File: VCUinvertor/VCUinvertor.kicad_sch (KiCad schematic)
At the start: 127 parts, among them J7 PowerSupply, J8 CAN_NXP, J9 BACKLIGHT, Q11 MMBT3904, Q12 IRLML6402, Q13 MMBT3904, Q14 IRLML6402, Q17 MMBT3904, Q18 MMBT3904, Q19 MMBT3904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

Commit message: FirstLayout_Completed
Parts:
- removed NXP11: NXP11, Connector_PinHeader_2.54mm:PinHeader_2x08_P2.54mm_Vertical, symbol Connector_Generic:Conn_02x10_Odd_Even
- removed NXP13: NXP13, Connector_PinHeader_2.54mm:PinHeader_2x10_P2.54mm_Vertical, symbol Connector_Generic:Conn_02x10_Odd_Even
- removed NXP14: NXP14, Connector_PinHeader_2.54mm:PinHeader_2x10_P2.54mm_Vertical, symbol Connector_Generic:Conn_02x10_Odd_Even
- removed Q11, Q13, Q17, Q18, Q19, Q23, Q25, Q27, Q29, Q41: MMBT3904, Package_TO_SOT_SMD:SOT-23, symbol Transistor_BJT:MMBT3904
- removed Q12, Q14, Q20, Q21, Q22, Q24, Q26, Q28, Q30, Q42: IRLML6402, Package_TO_SOT_SMD:SOT-23, symbol Transistor_FET:IRLML6402
- removed R29, R32, R33, R36, R41, R43, R45, R50, R51, R52, R53, R56, R57, R60, R61, R65, R68, R89, R92: 10k, Resistor_SMD:R_0805_2012Metric, symbol Device:R_Small
- removed R30, R34, R42, R44, R46, R54, R58, R62, R66, R90: 100k, Resistor_SMD:R_0805_2012Metric, symbol Device:R_Small
- removed R31, R35, R47, R48, R49, R55, R59, R67, R91: 100, Resistor_SMD:R_0805_2012Metric, symbol Device:R_Small
- added NXP11: NXP11, Connector_PinHeader_2.54mm:PinHeader_2x08_P2.54mm_Vertical, symbol Connector_Generic:Conn_02x08_Odd_Even
- added NXP13: NXP13, Connector_PinHeader_2.54mm:PinHeader_2x08_P2.54mm_Vertical, symbol Connector_Generic:Conn_02x08_Odd_Even
- added NXP14: NXP14, Connector_PinHeader_2.54mm:PinHeader_2x08_P2.54mm_Vertical, symbol Connector_Generic:Conn_02x08_Odd_Even
- added Q1, Q10, Q2, Q3, Q4, Q5, Q6, Q7, Q8, Q9: 2N7002, Package_TO_SOT_SMD:SOT-23, symbol Transistor_FET:2N7002
- added R10, R11, R12, R13, R14, R15, R16, R17, R18, R19, R20, R21, R22, R5, R6, R7, R8, R9: 10k, Resistor_SMD:R_0805_2012Metric, symbol Device:R_Small
- NXP10, NXP12: footprint Connector_PinHeader_2.54mm:PinHeader_2x08_P2.54mm_Vertical -> Connector_PinHeader_2.54mm:PinHeader_2x10_P2.54mm_Vertical
- R63: value 100 -> 10k
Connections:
- net V-1 is gone; now on net GND: JU1.4 (Pin_4)
- net V-2 is gone; now on net GND: JU2.4 (Pin_4)
- net +12V: now also NXP13.1 (Pin_1), R10.1, R12.1, R14.1, R16.1, R18.1, R20.1, R22.1, R6.1, R8.1
- net ACC1: now also Q2.3 (D), R6.2
- net ACC2: now also R64.2, Q1.3 (D)
- net BREAKLIGHT: now also NXP13.2 (Pin_2)
- net ECO1: now also Q3.3 (D), R8.2
- net ECO2: now also Q7.3 (D), R16.2
- net FWD1: now also Q5.3 (D), R12.2
- net FWD2: now also Q9.3 (D), R20.2
- net GND: now also U1.15 (GND), NXP13.13 (Pin_13), Q1.2 (S), Q10.2 (S), Q2.2 (S), Q3.2 (S), Q4.2 (S), Q5.2 (S), Q6.2 (S), Q7.2 (S), Q8.2 (S), Q9.2 (S)
- net H_Brk1: now also Q4.3 (D), R10.2
- net H_Brk2: now also Q8.3 (D), R18.2
- net NXP_ACC01: now also NXP12.20 (Pin_20), R5.1
- net NXP_ACC02: now also NXP10.14 (Pin_14), R63.1
- net NXP_BRK01: now also NXP12.5 (Pin_5), R9.1
- net NXP_BRK02: now also NXP10.10 (Pin_10), R17.1
- net NXP_ECO01: now also NXP12.18 (Pin_18), R7.1
- net NXP_ECO02: now also NXP10.12 (Pin_12), R15.1
- net NXP_FWD01: now also NXP12.4 (Pin_4), R11.1
- net NXP_FWD02: now also NXP10.8 (Pin_8), R19.1
- net NXP_REV01: now also NXP12.2 (Pin_2), R13.1
- net NXP_REV02: now also NXP10.6 (Pin_6), R21.1
- net NXP_TPSOUT01: now also NXP14.1 (Pin_1)
- net NXP_TPSOUT02: now also NXP14.3 (Pin_3)
- net REV1: now also Q6.3 (D), R14.2
- net REV2: now also Q10.3 (D), R22.2
- net Rx_UART01: now also NXP12.8 (Pin_8); no longer NXP12.2 (Pin_2)
- net Rx_UART02: now also NXP11.2 (Pin_2)
- net Tx_UART01: now also NXP12.6 (Pin_6); no longer NXP12.3 (Pin_3)
- net Tx_UART02: now also NXP11.3 (Pin_3)
- net at R63.2: now also Q1.1 (G)
- net V+1: no longer names the net of JU1.1 (Pin_1)
- net V+2: no longer names the net of JU2.1 (Pin_1)
- new net: Q7.1 (G), R15.2
- new net: Q6.1 (G), R13.2
- new net: Q9.1 (G), R19.2
- new net: Q4.1 (G), R9.2
- new net: Q5.1 (G), R11.2
- new net: Q2.1 (G), R5.2
- new net: Q3.1 (G), R7.2
- new net: Q10.1 (G), R21.2
- new net: Q8.1 (G), R17.2
- no-connect marks 85 -> 95
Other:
- moved on the sheet: CA1, J8, NXP10, NXP12, NXP15, R63, R64

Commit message: Pyy & Pzz pin assignment
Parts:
- renumbered J8 to J21
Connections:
- net Pyy: now also NXP11.16 (Pin_16)
- net Pzz: now also NXP11.4 (Pin_4)
- no-connect marks 95 -> 93
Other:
- note added: "J13 - pin: 1 & 15 (12V) J13 - pin: 13 (GND)"
- note removed: "J13 - 1 & 15 (12V) J13 - 13 (GND)"
- moved on the sheet: C1, C10, C11, C12, C2, C5, C6, C7, C8, C9, DAC1, JU1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

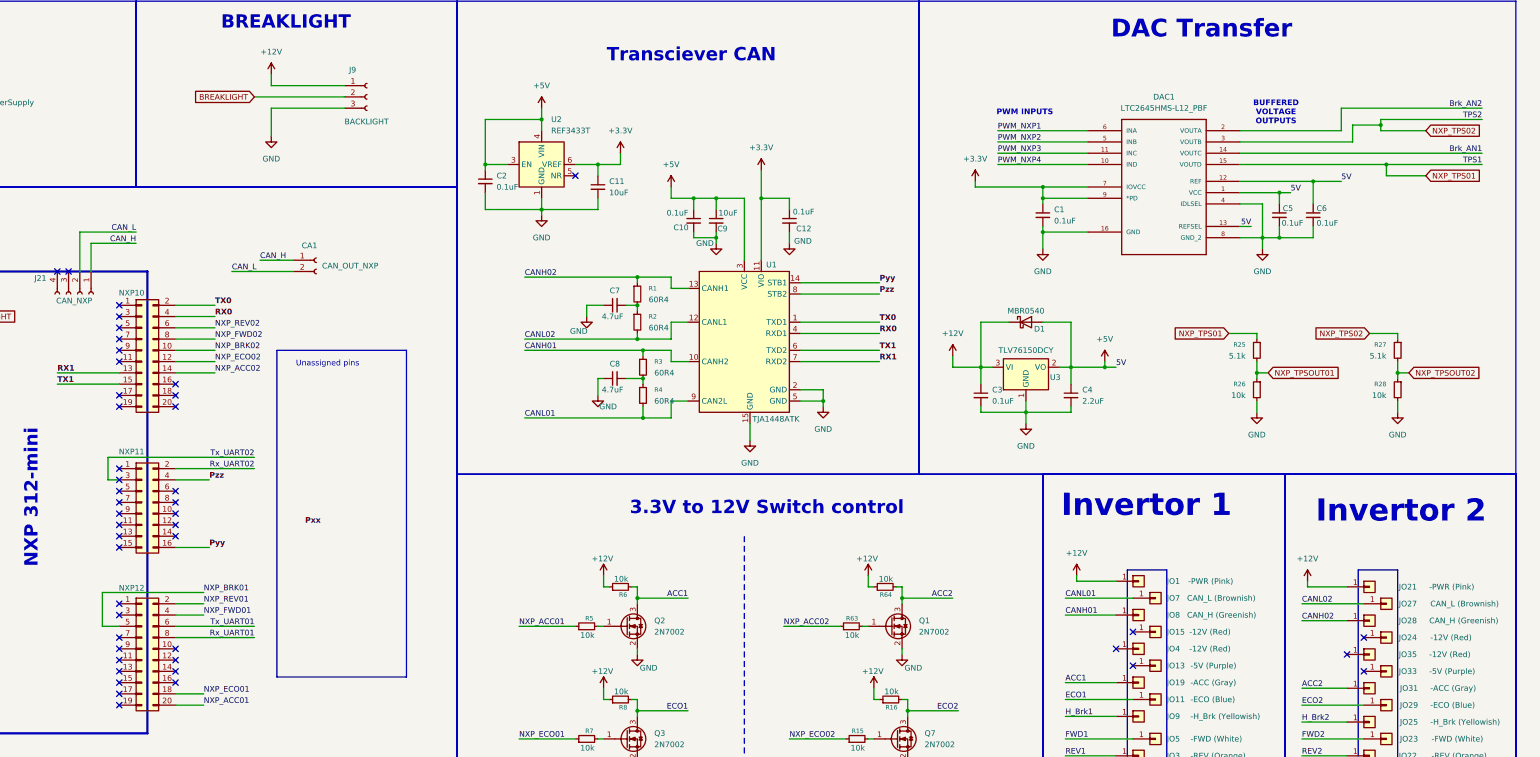
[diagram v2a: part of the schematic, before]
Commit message: Added datasheets for MOS
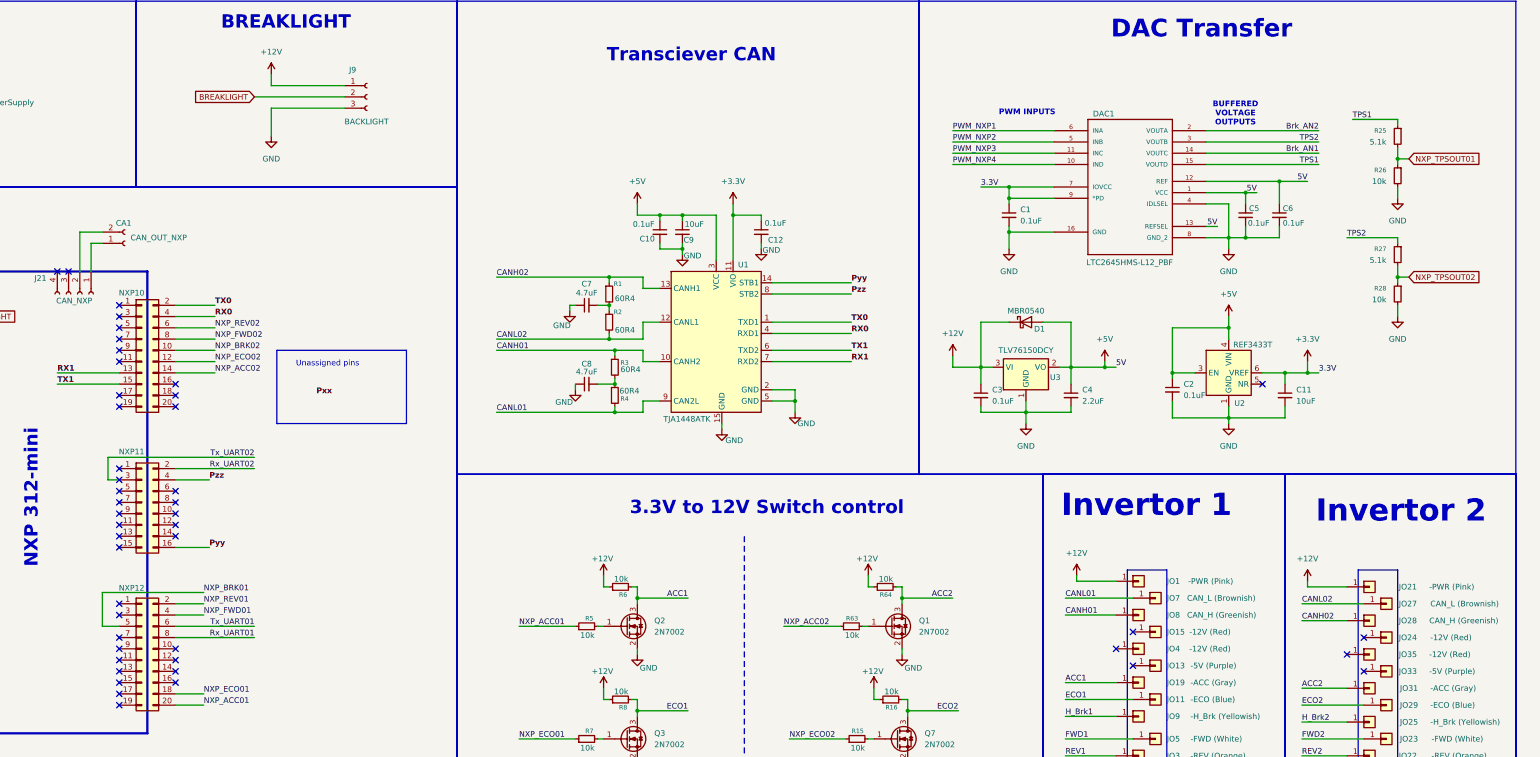
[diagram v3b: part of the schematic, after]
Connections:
- net CAN_H: no longer names the net of CA1.1 (Pin_1), J21.1 (Pin_1)
- net CAN_L: no longer names the net of CA1.2 (Pin_2), J21.2 (Pin_2)
- net NXP_TPS01 renamed TPS1
- net NXP_TPS02 renamed TPS2
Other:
- moved on the sheet: C1, C10, C11, C12, C2, C5, C6, C7, C8, C9, CA1, DAC1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

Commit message: LastCorrection_ToBeChecked
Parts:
- J7: footprint Connector_Phoenix_MSTB:PhoenixContact_MSTBVA_2,5_2-G-5,08_1x02_P5.08mm_Vertical -> Connector_JST:JST_PH_B2B-PH-K_1x02_P2.00mm_Vertical
- JO1, JO21: value -PWR (Pink) -> PWR (Pink)
- JO11, JO29: value -ECO (Blue) -> ECO (Blue)
- JO12, JO32: value -TPS (Green) -> TPS (Green)
- JO13, JO33: value -5V (Purple) -> 5V (Purple)
- JO14, JO26, JO34, JO6: value -GND (Black) -> GND (Black)
- JO15, JO24, JO35, JO4: value -12V (Red) -> 12V (Red)
- JO19, JO31: value -ACC (Gray) -> ACC (Gray)
- JO22, JO3: value -REV (Orange) -> REV (Orange)
- JO23, JO5: value -FWD (White) -> FWD (White)
- JO25, JO9: value -H_Brk (Yellowish) -> H_Brk (Yellowish)
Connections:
- net PWM_NXP1: now also NXP15.11 (Pin_11); no longer NXP15.9 (Pin_9)
- net PWM_NXP2: now also NXP15.9 (Pin_9); no longer NXP15.11 (Pin_11)
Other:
- moved on the sheet: C10, C12, C7, C8, C9, R1, R2, R3, R4, U1

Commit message: Block diagram cleanup
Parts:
- J9: value BACKLIGHT -> BREAKLIGHT
- renumbered J21 to CA0
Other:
- note added: "1. PWR(7): Controller power supply (input). ※Pink 2. REV_SW(14): Reverse switch input. ※Orange 3. GND(6): Signal return or power supply return. ※Black 4. FWD(12): Forward switch or can be enabled as High speed switch function. ※White 5. Throttle(3): Throttle analog input, 0-5V. ※ Green 6. Foot_SW(15): Throttle switch input. ※Gray 7. 12V(11): 12V Supply. ※Red 8. 12V (25): brake switch. ※Yellowish 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"
- note added: "3.3V + 5V sources"
- note added: "Check TJA1448 datasheet (page 24)"
- note added: "Invertor pin functionality"
- note added: "S32K312MINI-EVB"
- note added: "Signal reduction 5V to 3.3V"
- note added: "UART CONNECTION"
- note added: "using LTC2645HMS-L12_PBF"
- note added: "using TJA1448ATK"
- note removed: "NXP 312-mini"
- note removed: "UART Connections for INVERTERS"
- moved on the sheet: C1, C10, C11, C12, C2, C3, C4, C5, C6, C7, C8, C9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

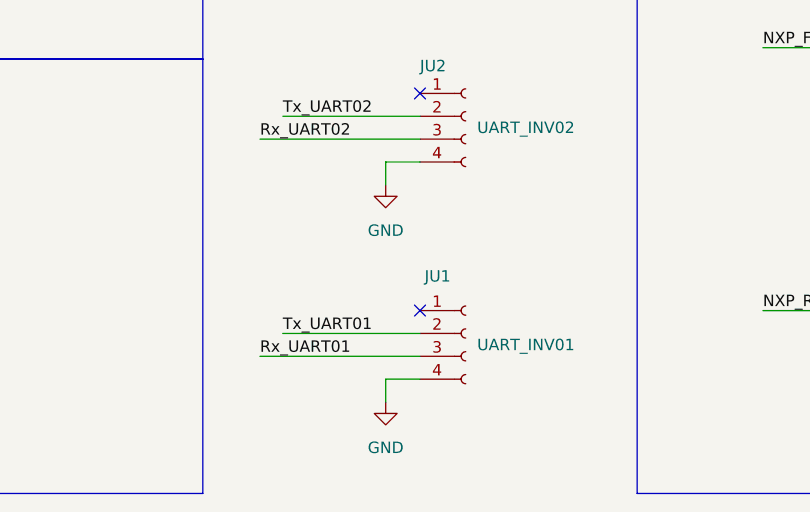
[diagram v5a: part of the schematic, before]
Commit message: BOM csv added
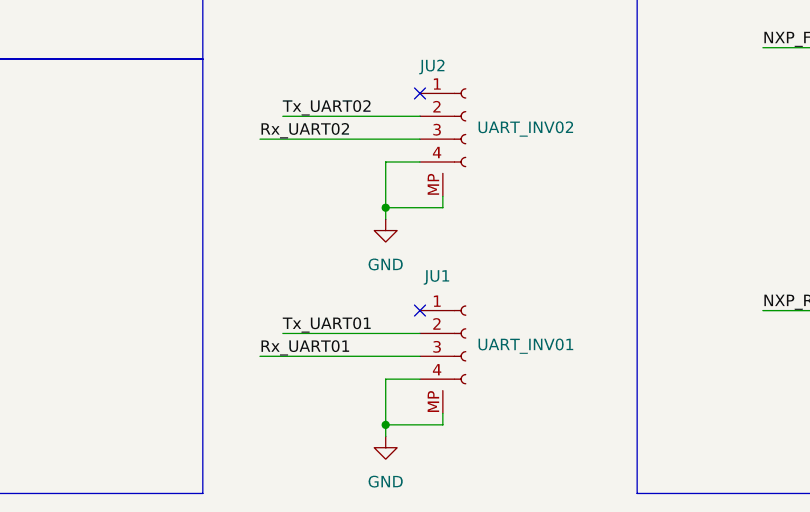
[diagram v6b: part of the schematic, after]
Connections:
- net GND: now also JU1.MP, JU2.MP
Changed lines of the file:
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@@
 	)
 	(junction
+		(at 139.7 276.86)
+		(diameter 0)
+		(color 0 0 0 0)
+	)
+	(junction
 		(at 269.24 228.6)
 		(diameter 0)
@@
 	)
 	(junction
+		(at 139.7 252.73)
+		(diameter 0)
+		(color 0 0 0 0)
+	)
+	(junction
 		(at 374.65 162.56)
 		(diameter 0)
@@
 	(wire
 		(pts
+			(xy 139.7 276.86) (xy 139.7 278.13)
+		)
+		(stroke
+			(width 0)
+			(type default)
+		)
+	)
+	(wire
+		(pts
 			(xy 218.44 59.69) (xy 218.44 60.96)
 		)
@@
 	(wire
 		(pts
+			(xy 139.7 252.73) (xy 139.7 254)
+		)
+		(stroke
+			(width 0)
+			(type default)
+		)
+	)
+	(wire
+		(pts
 			(xy 104.14 114.3) (xy 121.92 114.3)
 		)
@@
 	(wire
 		(pts
-			(xy 139.7 247.65) (xy 139.7 250.19)
+			(xy 139.7 247.65) (xy 139.7 252.73)
 		)
 		(stroke
@@
 	(wire
 		(pts
+			(xy 146.05 276.86) (xy 139.7 276.86)
+		)
+		(stroke
+			(width 0)
+			(type default)
+		)
+	)
+	(wire
+		(pts
 			(xy 137.16 171.45) (xy 137.16 168.91)
 		)
@@
 	(wire
 		(pts
-			(xy 139.7 271.78) (xy 139.7 274.32)
+			(xy 139.7 271.78) (xy 139.7 276.86)
 		)
 		(stroke
@@
 	(wire
 		(pts
+			(xy 146.05 252.73) (xy 139.7 252.73)
+		)
+		(stroke
+			(width 0)
+			(type default)
+		)
+	)
+	(wire
+		(pts
 			(xy 260.35 234.95) (xy 261.62 234.95)
 		)
@@
 	(wire
 		(pts
+			(xy 146.05 251.46) (xy 146.05 252.73)
+		)
+		(stroke
+			(width 0)
+			(type default)
+		)
+	)
+	(wire
+		(pts
 			(xy 392.43 152.4) (xy 387.35 152.4)
 		)
@@
 	(wire
 		(pts
+			(xy 146.05 275.59) (xy 146.05 276.86)
+		)
+		(stroke
+			(width 0)
+			(type default)
+		)
+	)
+	(wire
+		(pts
 			(xy 213.36 52.07) (xy 218.44 52.07)
 		)
@@
 	(symbol
 		(lib_id "power:GND")
-		(at 139.7 274.32 0)
+		(at 139.7 278.13 0)
 		(unit 1)
 		(exclude_from_sim no)
@@
 		(fields_autoplaced yes)
 		(property "Reference" "#PWR041"
-			(at 139.7 280.67 0)
+			(at 139.7 284.48 0)
 			(effects
 				(font
@@
 		)
 		(property "Value" "GND"
-			(at 139.7 279.4 0)
+			(at 139.7 283.21 0)
 			(effects
 				(font
@@
 		)
 		(property "Footprint" ""
-			(at 139.7 274.32 0)
+			(at 139.7 278.13 0)
 			(effects
 				(font
@@
 		)
 		(property "Datasheet" ""
-			(at 139.7 274.32 0)
+			(at 139.7 278.13 0)
 			(effects
 				(font
@@
 		)
 		(property "Description" "Power symbol creates a global label with name \"GND\" , ground"
-			(at 139.7 274.32 0)
+			(at 139.7 278.13 0)
 			(effects
 				(font
@@
 	(symbol
 		(lib_id "power:GND")
-		(at 139.7 250.19 0)
+		(at 139.7 254 0)
 		(unit 1)
 		(exclude_from_sim no)
@@
 		(fields_autoplaced yes)
 		(property "Reference" "#PWR040"
-			(at 139.7 256.54 0)
+			(at 139.7 260.35 0)
 			(effects
 				(font
@@
 		)
 		(property "Value" "GND"
-			(at 139.7 255.27 0)
+			(at 139.7 259.08 0)
 			(effects
 				(font
@@
 		)
 		(property "Footprint" ""
-			(at 139.7 250.19 0)
+			(at 139.7 254 0)
 			(effects
 				(font
@@
 		)
 		(property "Datasheet" ""
-			(at 139.7 250.19 0)
+			(at 139.7 254 0)
 			(effects
 				(font
@@
 		)
 		(property "Description" "Power symbol creates a global label with name \"GND\" , ground"
-			(at 139.7 250.19 0)
+			(at 139.7 254 0)
 			(effects
 				(font
@@
 	)
 	(symbol
+		(lib_name "Conn_01x04_Socket_1")
 		(lib_id "Connector:Conn_01x04_Socket")
 		(at 148.59 242.57 0)
@@
 		(pin "4"
 		)
+		(pin "MP"
+		)
 		(instances
 			(project "VCUinvertor"
@@
 	)
 	(symbol
+		(lib_name "Conn_01x04_Socket_2")
 		(lib_id "Connector:Conn_01x04_Socket")
 		(at 148.59 266.7 0)
@@
 		(pin "4"
 		)
+		(pin "MP"
+		)
 		(instances

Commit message: Changes on Supply
1.Protection shottky diode added
2.Separate supply for INV via Darlington (1A Max.)
3.Control of the supply from J10 Pin 20 for INV supply - added
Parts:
- added D2: MBRS340, Diode_SMD:D_SMC, symbol Diode:MBRS340
- added H1, H2, H3, H4: MountingHole_Pad, MountingHole:MountingHole_3.2mm_M3_ISO14580_Pad, symbol Mechanical:MountingHole_Pad
- added Q11: BC848, Package_TO_SOT_SMD:SOT-23, symbol Transistor_BJT:BC848
- added Q12: BCP51, Package_TO_SOT_SMD:SOT-223-3_TabPin2, symbol Transistor_BJT:BCP51
- added R23: 10k, Resistor_SMD:R_0805_2012Metric, symbol Device:R_Small
- added R24: 1k, Resistor_SMD:R_0805_2012Metric, symbol Device:R_Small
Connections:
- net +12V: now also D2.1 (K), Q12.2 (C), R24.2; no longer JO1.1 (Pin_1), JO21.1 (Pin_1)
- net GND: now also JO26.1 (Pin_1), JO6.1 (Pin_1), D2.2 (A), H1.1, H2.1, H3.1, H4.1
- net INV_OFF: now reaches NXP10.20 (Pin_20)
- net INV_OFF: now also R23.1
- new net: Q11.1 (B), R23.2
- new net: Q11.2 (E), Q12.1 (B)
- new net: Q11.3 (C), R24.1
- new net INV_Supply: JO1.1 (Pin_1), JO21.1 (Pin_1), Q12.3 (E)
- no-connect marks 93 -> 90
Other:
- note removed: "Check TJA1448 datasheet (page 24)"
- note removed: "Unassigned pins"
- moved on the sheet: CA0, CA1

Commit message: BOM + Gerbers - added
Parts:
- J9: value BREAKLIGHT -> BRAKE LIGHT
- Q11: value BC848 -> BC848C
- R23: value 10k -> 1.7k
- R24: value 1k -> 360R
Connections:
- net BREAKLIGHT renamed BRAKELIGHT
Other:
- note added: "BRAKE LIGHT"
- note added: "Inverter supply path"
- note removed: "BREAKLIGHT"
- moved on the sheet: H1, H2, H3, H4, JU1, JU2, Q11, Q12, R23, R24, R25, R26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
